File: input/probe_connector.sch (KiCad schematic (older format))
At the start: 7 parts, among them J1 Sensor

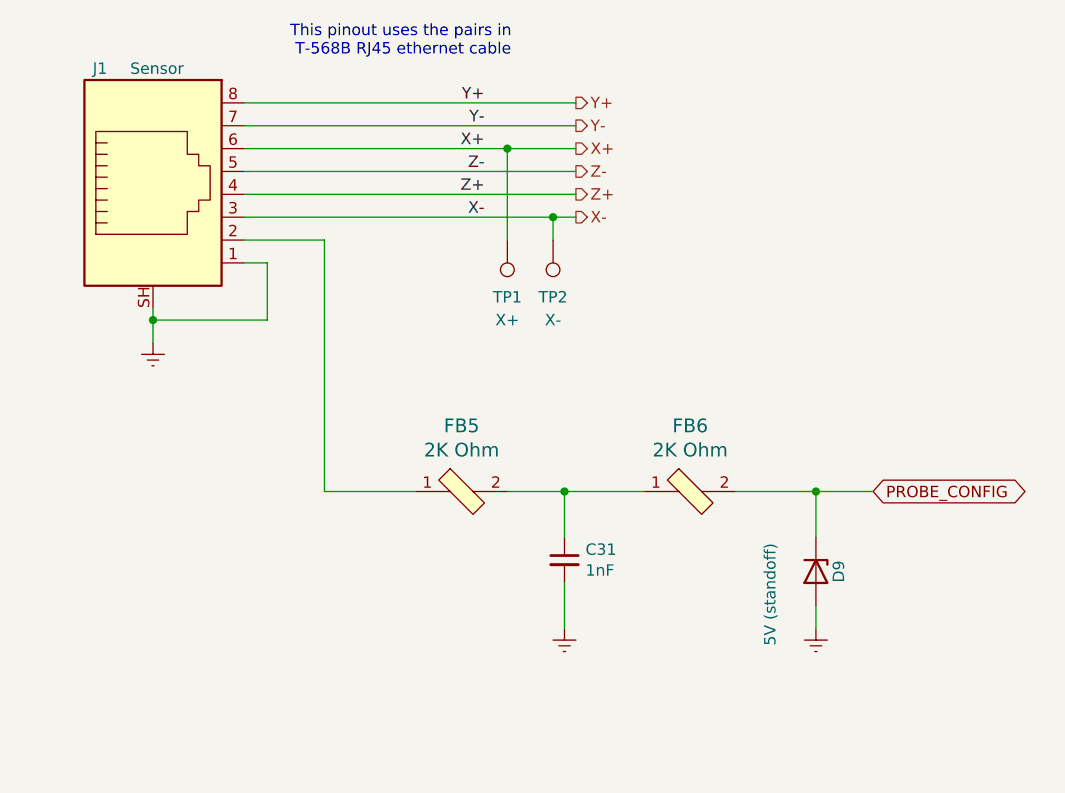
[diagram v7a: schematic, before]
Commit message: Start of in_panel design, for input connectors on front panel, with RFI/ESD protection.  These components moved from input_board.
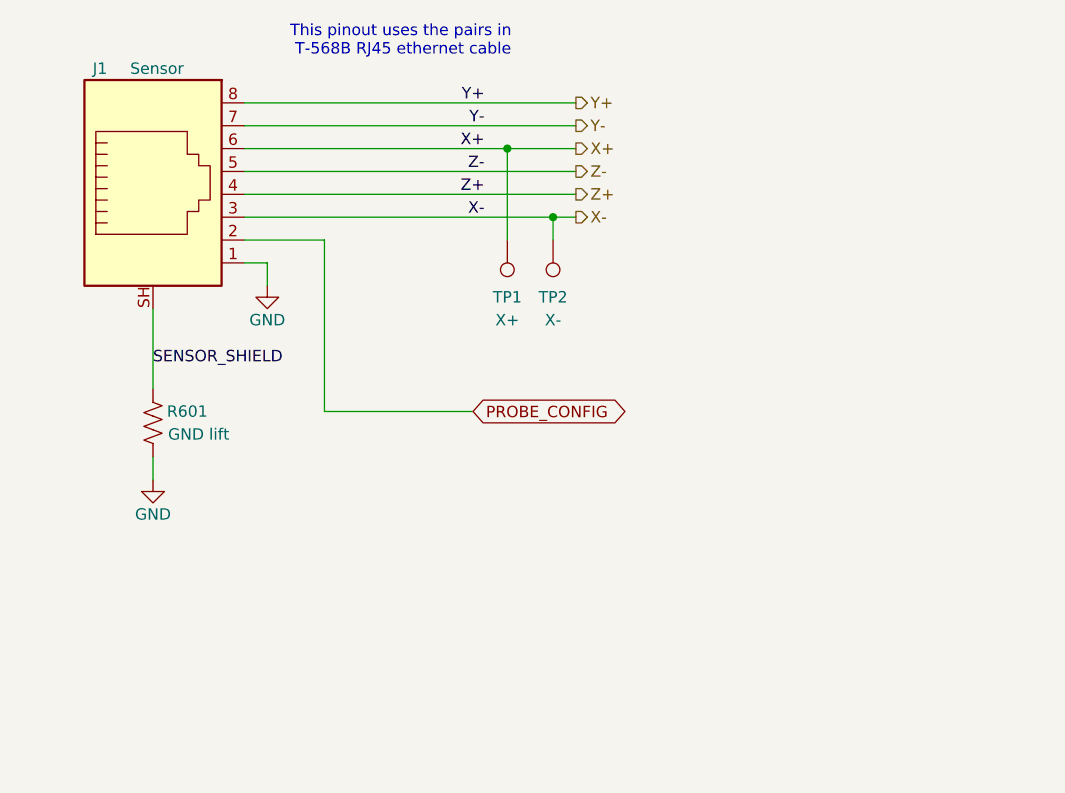
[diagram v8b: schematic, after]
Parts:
- removed C31: 1nF, Capacitor_SMD:C_0805_2012Metric, symbol Device:C_Small
- removed D9: 5V (standoff), Diode_SMD:D_SMA, symbol Device:D_Zener
- removed FB5, FB6: 2K Ohm, Inductor_SMD:L_0805_2012Metric, symbol dk_Ferrite-Beads-and-Chips:MPZ2012S601AT000
- added R601: GND lift, Resistor_SMD:R_0603_1608Metric, symbol Device:R_US
- J1: footprint Connector_RJ:RJ45_Amphenol_RJHSE538X -> input:RJ45_Amphenol_RJHSE5380
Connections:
- net PROBE_CONFIG: now also J1.2
- net Earth renamed GND
- net GND: now also R601.1; no longer J1.SH
- new net SENSOR_SHIELD: J1.SH, R601.2
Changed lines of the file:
@@
 Comment4 ""
 $EndDescr
-Wire Wire Line
-	2650 3250 2650 3300
 $Comp
 L Connector:RJ45_Shielded J?
@@
 F 0 "J1" H 2450 3300 50  0000 R CNN
 F 1 "Sensor" H 2550 3300 50  0000 L CNN
-F 2 "Connector_RJ:RJ45_Amphenol_RJHSE538X" V 2650 2775 50  0001 C CNN
+F 2 "input:RJ45_Amphenol_RJHSE5380" V 2650 2775 50  0001 C CNN
 F 3 "https://cdn.amphenol-icc.com/media/wysiwyg/files/drawing/rjhse538x.pdf" V 2650 2775 50  0001 C CNN
 F 4 "RJHSE5387-ND" H 2650 2750 50  0001 C CNN "Digikey"
@@
 	1    0    0    -1
 $EndComp
-Text GLabel 5800 4050 2    50   BiDi ~ 0
+Text GLabel 4050 3700 2    50   BiDi ~ 0
 PROBE_CONFIG
 Wire Wire Line
 	3050 3050 3150 3050
-Wire Wire Line
-	3150 3050 3150 3300
-Wire Wire Line
-	3150 3300 2650 3300
-Connection ~ 2650 3300
-Wire Wire Line
-	2650 3300 2650 3400
 Wire Wire Line
 	3050 2350 4500 2350
@@
 Text Label 4100 2350 2    50   ~ 0
 Y+
-$Comp
-L dk_Ferrite-Beads-and-Chips:MPZ2012S601AT000 FB?
-U 1 1 5E75F20B
-P 4000 4050
-AR Path="/5DFCF14D/5DE42731/5E75F20B" Ref="FB?"  Part="1"
-AR Path="/5E756356/5E75F20B" Ref="FB5"  Part="1"
-AR Path="/5E624B3C/5E756356/5E75F20B" Ref="FB5"  Part="1"
-F 0 "FB5" H 4000 4337 60  0000 C CNN
-F 1 "2K Ohm" H 4000 4231 60  0000 C CNN
-F 2 "Inductor_SMD:L_0805_2012Metric" H 4200 4250 60  0001 L CNN
-F 3 "https://assets.lairdtech.com/home/brandworld/files/Catalog_EMI%20FILTERING%20RF%200717.pdf" H 4200 4350 60  0001 L CNN
-F 4 " 240-2396-1-ND" H 4200 4450 60  0001 L CNN "Digi-Key_PN"
-F 5 "HZ0805C202R-10" H 4200 4550 60  0001 L CNN "MPN"
-F 6 "Filters" H 4200 4650 60  0001 L CNN "Category"
-F 7 "Ferrite Beads and Chips" H 4200 4750 60  0001 L CNN "Family"
-F 8 "https://product.tdk.com/info/en/catalog/datasheets/beads_commercial_power_mpz2012_en.pdf" H 4200 4850 60  0001 L CNN "DK_Datasheet_Link"
-F 9 "/product-detail/en/tdk-corporation/MPZ2012S601AT000/445-2206-1-ND/765104" H 4200 4950 60  0001 L CNN "DK_Detail_Page"
-F 10 "FERRITE BEAD 2 KOHM 0805 1LN" H 4200 5050 60  0001 L CNN "Description"
-F 11 "Laird-Signal Integrity Products" H 4200 5150 60  0001 L CNN "Manufacturer"
-F 12 "Active" H 4200 5250 60  0001 L CNN "Status"
-F 13 "5" H 4000 4050 50  0001 C CNN "DK line"
-F 14 "240-2396-1-ND" H 4000 4050 50  0001 C CNN "Digikey"
-	1    4000 4050
-	1    0    0    -1
-$EndComp
 Wire Wire Line
-	3400 4050 3800 4050
-Wire Wire Line
-	3400 2950 3400 4050
+	3400 2950 3400 3700
 Wire Wire Line
 	3050 2950 3400 2950
-$Comp
-L Device:D_Zener D?
-U 1 1 5E7695B8
-P 5550 4400
-AR Path="/5E51E83D/5E7695B8" Ref="D?"  Part="1"
-AR Path="/5E756356/5E7695B8" Ref="D9"  Part="1"
-AR Path="/5E624B3C/5E756356/5E7695B8" Ref="D9"  Part="1"
-F 0 "D9" H 5550 4500 50  0000 C CNN
-F 1 "5V (standoff)" H 5650 4200 50  0000 C CNN
-F 2 "Diode_SMD:D_SMA" H 5550 4400 50  0001 C CNN
-F 3 "https://katalog.we-online.de/pbs/datasheet/824500500.pdf" H 5550 4400 50  0001 C CNN
-F 4 "824500500" H 5550 4400 50  0001 C CNN "MPN"
-F 5 "TVS DIODE 5V 9.2V DO214AC" H 5550 4400 50  0001 C CNN "Description"
-F 6 "732-9974-1-ND" H 5550 4400 50  0001 C CNN "Digikey"
-F 7 "40" H 5550 4400 50  0001 C CNN "DK line"
-F 8 "Würth Elektronik" H 5550 4400 50  0001 C CNN "Manufacturer"
-	1    5550 4400
-	0    1    1    0
-$EndComp
-Wire Wire Line
-	5550 4050 5550 4250
-Wire Wire Line
-	5550 4550 5550 4650
-$Comp
-L dk_Ferrite-Beads-and-Chips:MPZ2012S601AT000 FB?
-U 1 1 5E76B461
-P 5000 4050
-AR Path="/5DFCF14D/5DE42731/5E76B461" Ref="FB?"  Part="1"
-AR Path="/5E756356/5E76B461" Ref="FB6"  Part="1"
-AR Path="/5E624B3C/5E756356/5E76B461" Ref="FB6"  Part="1"
-F 0 "FB6" H 5000 4337 60  0000 C CNN
-F 1 "2K Ohm" H 5000 4231 60  0000 C CNN
-F 2 "Inductor_SMD:L_0805_2012Metric" H 5200 4250 60  0001 L CNN
-F 3 "https://assets.lairdtech.com/home/brandworld/files/Catalog_EMI%20FILTERING%20RF%200717.pdf" H 5200 4350 60  0001 L CNN
-F 4 " 240-2396-1-ND" H 5200 4450 60  0001 L CNN "Digi-Key_PN"
-F 5 "HZ0805C202R-10" H 5200 4550 60  0001 L CNN "MPN"
-F 6 "Filters" H 5200 4650 60  0001 L CNN "Category"
-F 7 "Ferrite Beads and Chips" H 5200 4750 60  0001 L CNN "Family"
-F 8 "https://product.tdk.com/info/en/catalog/datasheets/beads_commercial_power_mpz2012_en.pdf" H 5200 4850 60  0001 L CNN "DK_Datasheet_Link"
-F 9 "/product-detail/en/tdk-corporation/MPZ2012S601AT000/445-2206-1-ND/765104" H 5200 4950 60  0001 L CNN "DK_Detail_Page"
-F 10 "FERRITE BEAD 2 KOHM 0805 1LN" H 5200 5050 60  0001 L CNN "Description"
-F 11 "Laird-Signal Integrity Products" H 5200 5150 60  0001 L CNN "Manufacturer"
-F 12 "Active" H 5200 5250 60  0001 L CNN "Status"
-F 13 "5" H 5000 4050 50  0001 C CNN "DK line"
-F 14 "240-2396-1-ND" H 5000 4050 50  0001 C CNN "Digikey"
-	1    5000 4050
-	1    0    0    -1
-$EndComp
-$Comp
-L Device:C_Small C?
-U 1 1 5E76E2C4
-P 4450 4350
-AR Path="/5DFCF14D/5DE42731/5E76E2C4" Ref="C?"  Part="1"
-AR Path="/5E756356/5E76E2C4" Ref="C31"  Part="1"
-AR Path="/5E624B3C/5E756356/5E76E2C4" Ref="C31"  Part="1"
-F 0 "C31" H 4542 4396 50  0000 L CNN
-F 1 "1nF" H 4542 4305 50  0000 L CNN
-F 2 "Capacitor_SMD:C_0805_2012Metric" H 4450 4350 50  0001 C CNN
-F 3 "https://media.digikey.com/pdf/Data%20Sheets/Yageo%20PDFs/CCseries_mlcc_2002.pdf" H 4450 4350 50  0001 C CNN
-F 4 "311-3585-1-ND" H 4450 4350 50  0001 C CNN "Digikey"
-F 5 "CC0805FRNPO0BN102" H 4450 4350 50  0001 C CNN "MPN"
-F 6 "CAP CER 1000PF 100V NPO 0805" H 4450 4350 50  0001 C CNN "Description"
-F 7 "1" H 4450 4350 50  0001 C CNN "DK line"
-F 8 "Yageo" H 4450 4350 50  0001 C CNN "Manufacturer"
-	1    4450 4350
-	1    0    0    -1
-$EndComp
-Wire Wire Line
-	4200 4050 4450 4050
-Wire Wire Line
-	4450 4250 4450 4050
-Connection ~ 4450 4050
-Wire Wire Line
-	4450 4050 4800 4050
-Wire Wire Line
-	4450 4450 4450 4650
-Wire Wire Line
-	5200 4050 5550 4050
-Wire Wire Line
-	5800 4050 5550 4050
-Connection ~ 5550 4050
 Text Notes 3250 2150 0    50   ~ 0
 This pinout uses the pairs in \n T-568B RJ45 ethernet cable
@@
 Text HLabel 4500 2850 2    50   Output ~ 0
 X-
-$Comp
-L power:Earth #PWR059
-U 1 1 5E36FAA0
-P 2650 3400
-F 0 "#PWR059" H 2650 3150 50  0001 C CNN
-F 1 "Earth" H 2650 3250 50  0001 C CNN
-F 2 "" H 2650 3400 50  0001 C CNN
-F 3 "~" H 2650 3400 50  0001 C CNN
-	1    2650 3400
-	1    0    0    -1
-$EndComp
-$Comp
-L power:Earth #PWR060
-U 1 1 5E36FFC7
-P 4450 4650
-F 0 "#PWR060" H 4450 4400 50  0001 C CNN
-F 1 "Earth" H 4450 4500 50  0001 C CNN
-F 2 "" H 4450 4650 50  0001 C CNN
-F 3 "~" H 4450 4650 50  0001 C CNN
-	1    4450 4650
-	1    0    0    -1
-$EndComp
-$Comp
-L power:Earth #PWR061
-U 1 1 5E370459
-P 5550 4650
-F 0 "#PWR061" H 5550 4400 50  0001 C CNN
-F 1 "Earth" H 5550 4500 50  0001 C CNN
-F 2 "" H 5550 4650 50  0001 C CNN
-F 3 "~" H 5550 4650 50  0001 C CNN
-	1    5550 4650
-	1    0    0    -1
-$EndComp
 $Comp
 L Connector:TestPoint TP?
@@
 Wire Wire Line
 	4400 2850 4500 2850
+Wire Wire Line
+	4050 3700 3400 3700
+Wire Wire Line
+	3150 3050 3150 3150
+$Comp
+L power:GND #PWR?
+U 1 1 600B450F
+P 3150 3150
+AR Path="/600B450F" Ref="#PWR?"  Part="1"
+AR Path="/5E756356/600B450F" Ref="#PWR0125"  Part="1"
+F 0 "#PWR0125" H 3150 2900 50  0001 C CNN
+F 1 "GND" H 3150 3000 50  0000 C CNN
+F 2 "" H 3150 3150 50  0001 C CNN
+F 3 "" H 3150 3150 50  0001 C CNN
+	1    3150 3150
+	1    0    0    -1
+$EndComp
+$Comp
+L power:GND #PWR?
+U 1 1 600BE065
+P 2650 4000
+AR Path="/600BE065" Ref="#PWR?"  Part="1"
+AR Path="/5E756356/600BE065" Ref="#PWR0126"  Part="1"
+F 0 "#PWR0126" H 2650 3750 50  0001 C CNN
+F 1 "GND" H 2650 3850 50  0000 C CNN
+F 2 "" H 2650 4000 50  0001 C CNN
+F 3 "" H 2650 4000 50  0001 C CNN
+	1    2650 4000
+	1    0    0    -1
+$EndComp
+Wire Wire Line
+	2650 3250 2650 3600
+$Comp
+L Device:R_US R?
+U 1 1 600BA0A9
+P 2650 3750
+AR Path="/5DFCF14D/5DA78BF5/600BA0A9" Ref="R?"  Part="1"
+AR Path="/5DFCF14D/5E195558/600BA0A9" Ref="R?"  Part="1"
+AR Path="/5DFCF14D/5DA78AA2/600BA0A9" Ref="R?"  Part="1"
+AR Path="/5E448095/5DA78AA2/600BA0A9" Ref="R?"  Part="1"
+AR Path="/5E45936E/5DA78AA2/600BA0A9" Ref="R?"  Part="1"
+AR Path="/5E525F2C/5E6427A0/5DA78AA2/600BA0A9" Ref="R?"  Part="1"
+AR Path="/5E624B3C/5DFCF14D/5DA78AA2/600BA0A9" Ref="R?"  Part="1"
+AR Path="/5E624B3C/5E448095/5DA78AA2/600BA0A9" Ref="R?"  Part="1"
+AR Path="/5E624B3C/5E45936E/5DA78AA2/600BA0A9" Ref="R?"  Part="1"
+AR Path="/5E62FD57/5DFCF14D/5DA78AA2/600BA0A9" Ref="R?"  Part="1"
+AR Path="/5E62FD57/5E448095/5DA78AA2/600BA0A9" Ref="R?"  Part="1"
+AR Path="/5E62FD57/5E45936E/5DA78AA2/600BA0A9" Ref="R?"  Part="1"
+AR Path="/5E756356/600BA0A9" Ref="R601"  Part="1"
+F 0 "R601" H 2500 3700 50  0000 C CNN
+F 1 "GND lift" H 2450 3800 50  0000 C CNN
+F 2 "Resistor_SMD:R_0603_1608Metric" V 2690 3740 50  0001 C CNN
+F 3 "" H 2650 3750 50  0001 C CNN
+F 4 "Do Not Populate" H 2650 3750 50  0001 C CNN "Description"
+F 5 "DNP" H 2650 3750 50  0001 C CNN "MPN"
+	1    2650 3750
+	-1   0    0    1
+$EndComp
+Wire Wire Line
+	2650 3900 2650 4000
+Text Label 2650 3500 0    50   ~ 0
+SENSOR_SHIELD
 $EndSCHEMATC
